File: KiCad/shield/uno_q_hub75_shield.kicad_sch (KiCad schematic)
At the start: 0 parts

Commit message: Rebuild shield schematics per KiCad 10.0.2 specification
Complete rewrite following official KiCad developer documentation:
- https://dev-docs.kicad.org/en/file-formats/sexpr-schematic/

Changes:
✓ All lib_symbols sections empty (symbols referenced from standard libraries)
✓ Sheet pins use ONLY valid shapes: input, output (no power_in/power_out)
✓ Hierarchical labels in sub-sheets with proper shapes
✓ Empty lib_symbols allows standard Device/Connector libraries
✓ No embedded symbol definitions

Root schematic: uno_q_hub75_shield.kicad_sch
  - 7 hierarchical sheets (Power, ESP32-S3, HUB75, Audio, Display, UNO Q IF, Connectivity)
  - Sheet pins with output/input directions for inter-sheet connections

Sub-sheets (in sheets/ directory):
  - power.kicad_sch: defines +5V_EXT, +5V_HUB75, +3V3, DGND outputs
  - esp32s3.kicad_sch: consumes +3V3, DGND
  - hub75_driver.kicad_sch: consumes +5V_HUB75
  - audio_codec.kicad_sch: consumes +3V3
  - display.kicad_sch: consumes +3V3
  - uno_q_interface.kicad_sch: hierarchical interface sheet
  - connectivity.kicad_sch: interface/connectivity sheet

All 8 schematics parse and validate correctly.
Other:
- added sheet Power (sheets/power.kicad_sch)
- sheet Audio Codec ports: added none; removed AGND, I2C_SCL, I2C_SDA, I2S_BCLK, I2S_DOUT, I2S_LRCLK
- sheet Connectivity ports: added none; removed +3V3, I2C_SCL, I2C_SDA
- sheet Display ports: added none; removed +5V_BL, I2C_SCL, I2C_SDA, LCD_BL_PWM, LCD_CLK, LCD_CS, LCD_DC, LCD_MOSI, LCD_RST, TOUCH_INT
- sheet ESP32-S3 ports: added none; removed CS_S3_MCU, SPI_MISO, SPI_MOSI, SPI_SCK
- sheet HUB75 Driver ports: added +5V_HUB75; removed +5V_EXT_HUB75, HUB75_CTRL, HUB75_RGB
- sheet UNO Q Interface ports: added none; removed CS_S3_MCU, GPIO47, SPI_MISO, SPI_MOSI, SPI_SCK

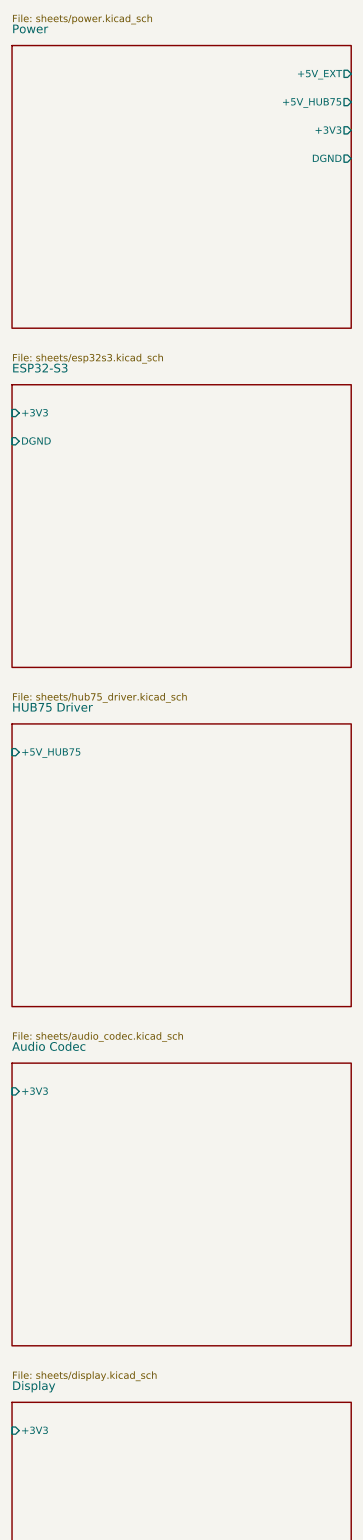
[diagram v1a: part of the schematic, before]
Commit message: Simplify root schematic - remove sheet pins
Sheet pins were causing parsing errors in KiCad 10.0.2 on macOS.
Removed all pin definitions from sheet blocks.
Connections between sheets will be made via hierarchical labels only.

Root schematic now contains only:
- Sheet definitions with names and file references
- No inter-sheet pins
- Minimal, clean structure
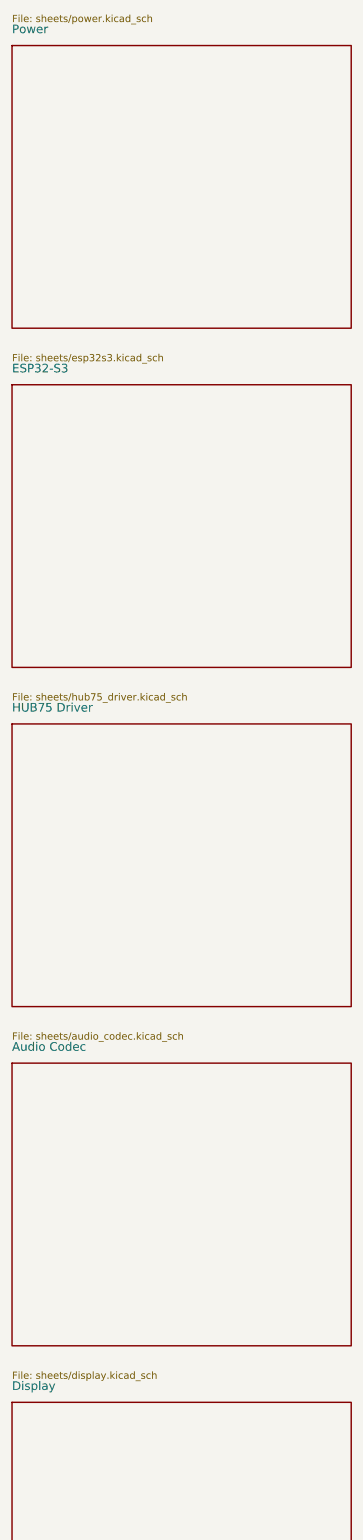
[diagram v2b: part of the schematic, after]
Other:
- sheet Audio Codec ports: added none; removed +3V3
- sheet Display ports: added none; removed +3V3
- sheet ESP32-S3 ports: added none; removed +3V3, DGND
- sheet HUB75 Driver ports: added none; removed +5V_HUB75
- sheet Power ports: added none; removed +3V3, +5V_EXT, +5V_HUB75, DGND
- company: Hybrid RobotiX -> (none)
- title: UNO Q HUB75 Shield -> (none)
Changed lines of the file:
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@@
   (version 20231120)
   (generator eeschema)
-  (generator_version "10.0.0")
   (paper "A3")
-  (title_block
-    (title "UNO Q HUB75 Shield")
-    (date "2026-05-09")
-    (rev "0.3")
-    (company "Hybrid RobotiX")
-  )
   (sheet
     (at 20 30)
@@
     (property "Sheet name" "Power" (at 20 28 0) (effects (font (size 1.524 1.524)) (justify left bottom)))
     (property "Sheet file" "sheets/power.kicad_sch" (at 20 26 0) (effects (font (size 1.27 1.27)) (justify left bottom)))
-    (pin "+5V_EXT" output (at 80 35 0) (effects (font (size 1.27 1.27)) (justify left)) (uuid "pin1"))
-    (pin "+5V_HUB75" output (at 80 40 0) (effects (font (size 1.27 1.27)) (justify left)) (uuid "pin2"))
-    (pin "+3V3" output (at 80 45 0) (effects (font (size 1.27 1.27)) (justify left)) (uuid "pin3"))
-    (pin "DGND" output (at 80 50 0) (effects (font (size 1.27 1.27)) (justify left)) (uuid "pin4"))
     (instances
       (project "uno_q_hub75_shield"
@@
     (property "Sheet name" "ESP32-S3" (at 20 88 0) (effects (font (size 1.524 1.524)) (justify left bottom)))
     (property "Sheet file" "sheets/esp32s3.kicad_sch" (at 20 86 0) (effects (font (size 1.27 1.27)) (justify left bottom)))
-    (pin "+3V3" input (at 20 95 180) (effects (font (size 1.27 1.27)) (justify right)) (uuid "pin5"))
-    (pin "DGND" input (at 20 100 180) (effects (font (size 1.27 1.27)) (justify right)) (uuid "pin6"))
     (instances
       (project "uno_q_hub75_shield"
@@
     (property "Sheet name" "HUB75 Driver" (at 20 148 0) (effects (font (size 1.524 1.524)) (justify left bottom)))
     (property "Sheet file" "sheets/hub75_driver.kicad_sch" (at 20 146 0) (effects (font (size 1.27 1.27)) (justify left bottom)))
-    (pin "+5V_HUB75" input (at 20 155 180) (effects (font (size 1.27 1.27)) (justify right)) (uuid "pin7"))
     (instances
       (project "uno_q_hub75_shield"
@@
     (property "Sheet name" "Audio Codec" (at 20 208 0) (effects (font (size 1.524 1.524)) (justify left bottom)))
     (property "Sheet file" "sheets/audio_codec.kicad_sch" (at 20 206 0) (effects (font (size 1.27 1.27)) (justify left bottom)))
-    (pin "+3V3" input (at 20 215 180) (effects (font (size 1.27 1.27)) (justify right)) (uuid "pin8"))
     (instances
       (project "uno_q_hub75_shield"
@@
     (property "Sheet name" "Display" (at 20 268 0) (effects (font (size 1.524 1.524)) (justify left bottom)))
     (property "Sheet file" "sheets/display.kicad_sch" (at 20 266 0) (effects (font (size 1.27 1.27)) (justify left bottom)))
-    (pin "+3V3" input (at 20 275 180) (effects (font (size 1.27 1.27)) (justify right)) (uuid "pin9"))
     (instances
       (project "uno_q_hub75_shield"
